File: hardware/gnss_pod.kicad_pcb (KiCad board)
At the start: 2 copper layers, 240.3 x 213.8 mm, 19 parts, among them J1 SQT-110-01-L-D, J2 SSQ-126-04-G-D, J3 SSQ-126-04-G-D

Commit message: Some changes, wip usb, layout wip
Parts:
- removed MEC5, MEC6, MEC7, MEC8: M3, footprints_library_legacy:M3 hole
- added REF**: WR-MMCX_Wuerth_66012102111404_Vertical, Connector_Coaxial:WR-MMCX_Wuerth_66012102111404_Vertical, F.Cu at (157.5, 135.8)
- added REF**: MountingHole_3.5mm_Pad, MountingHole:MountingHole_3.5mm_Pad, F.Cu at (166.9, 72.3)
- added REF**: MountingHole_3.5mm_Pad, MountingHole:MountingHole_3.5mm_Pad, F.Cu at (132.6, 137.0)
- added REF**: MountingHole_3.5mm_Pad, MountingHole:MountingHole_3.5mm_Pad, F.Cu at (132.6, 72.3)
- added REF**: MountingHole_3.5mm_Pad, MountingHole:MountingHole_3.5mm_Pad, F.Cu at (166.9, 137.0)
- H1, H2, H3, H4, H5, H6, H7, H8: footprint MountingHole:MountingHole_6mm_Pad -> MountingHole:MountingHole_3mm_Pad
- moved H8 119.8 mm to (227.6, 124.3), turned to -90 degrees
- moved H6 107.7 mm to (227.6, 110.8), turned to -90 degrees
- moved H7 106.6 mm to (241.1, 124.3), turned to -90 degrees
- moved H4 97.9 mm to (227.6, 97.2), turned to -90 degrees
- moved H5 92.8 mm to (241.1, 110.8), turned to -90 degrees
- moved H2 91.1 mm to (227.6, 83.7), turned to -90 degrees
- moved H3 81.1 mm to (241.1, 97.2), turned to -90 degrees
- moved J1 75.2 mm to (159.0, 73.2)
- moved H1 72.7 mm to (241.1, 83.7), turned to -90 degrees
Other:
- board size 240.3 x 213.8 mm -> 89.1 x 92.1 mm

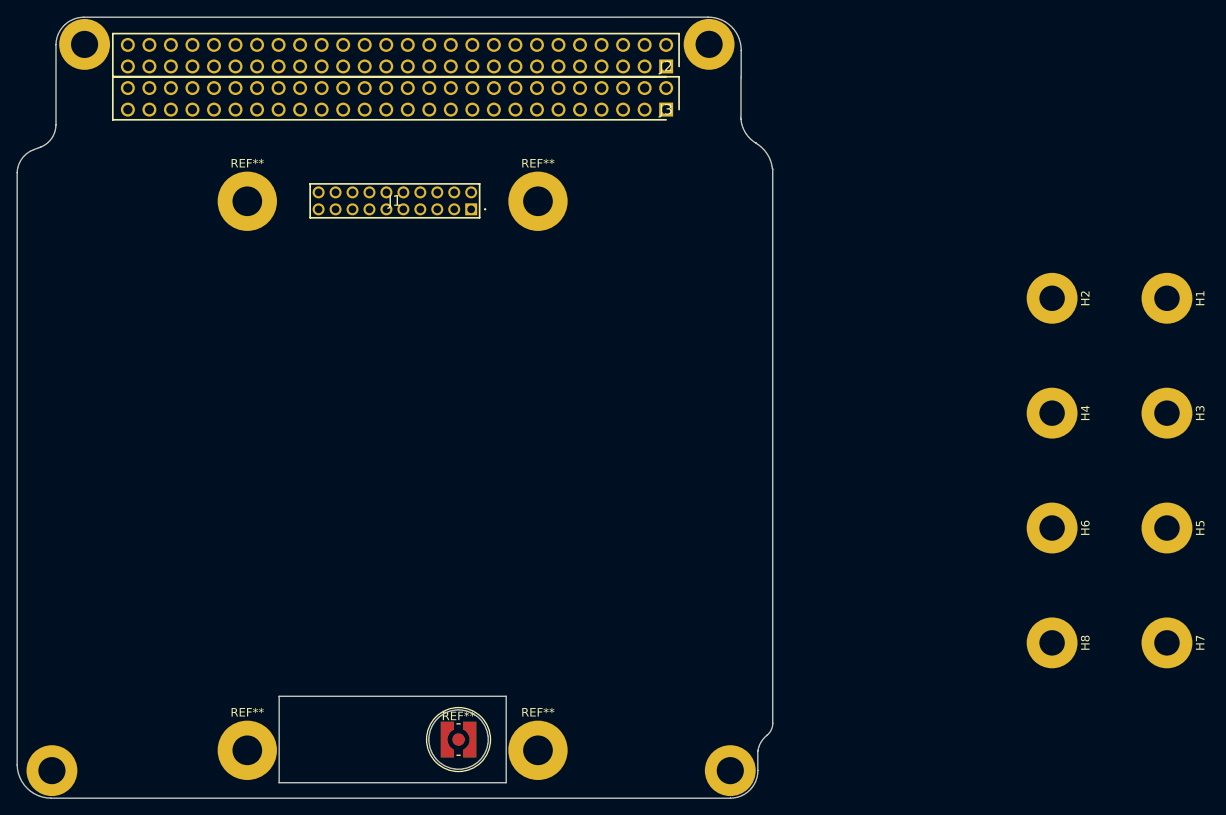
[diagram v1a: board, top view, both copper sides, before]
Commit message: Layout modified according to INEP requirements
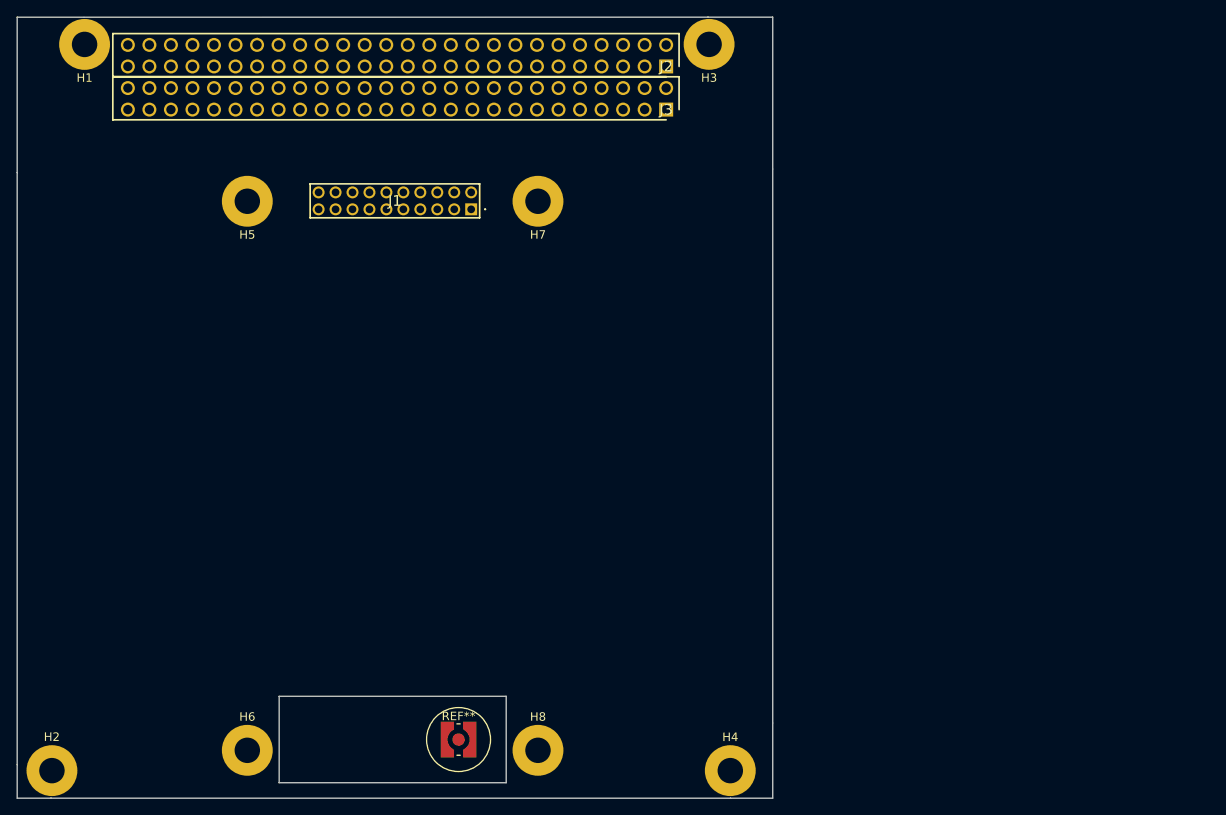
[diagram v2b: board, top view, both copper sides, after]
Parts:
- removed MEC1, MEC2, MEC3, MEC4: M3, footprints_library_legacy:M3 hole
- removed the REF** at (166.9, 72.3)
- removed the REF** at (132.6, 137.0)
- removed the REF** at (132.6, 72.3)
- removed the REF** at (166.9, 137.0)
- moved H1 131.2 mm to (113.4, 53.8), turned to 180 degrees
- moved H2 130.5 mm to (109.6, 139.4), turned to 180 degrees
- moved H5 115.1 mm to (132.6, 72.3), turned to 0 degrees
- moved H6 98.5 mm to (132.6, 137.0), turned to 0 degrees
- moved H7 90.7 mm to (166.9, 72.3), turned to 0 degrees
- moved H3 69.4 mm to (187.1, 53.7), turned to 180 degrees
- moved H8 62.0 mm to (166.9, 137.0), turned to 0 degrees
- moved H4 56.7 mm to (189.6, 139.4), turned to 180 degrees
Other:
- outline, holes or cut-outs redrawn
- board text added: "2x"
- board text added: "PROTOTYPE"
